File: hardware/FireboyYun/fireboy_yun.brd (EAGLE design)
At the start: 47.9 x 68.6 mm, 17 parts

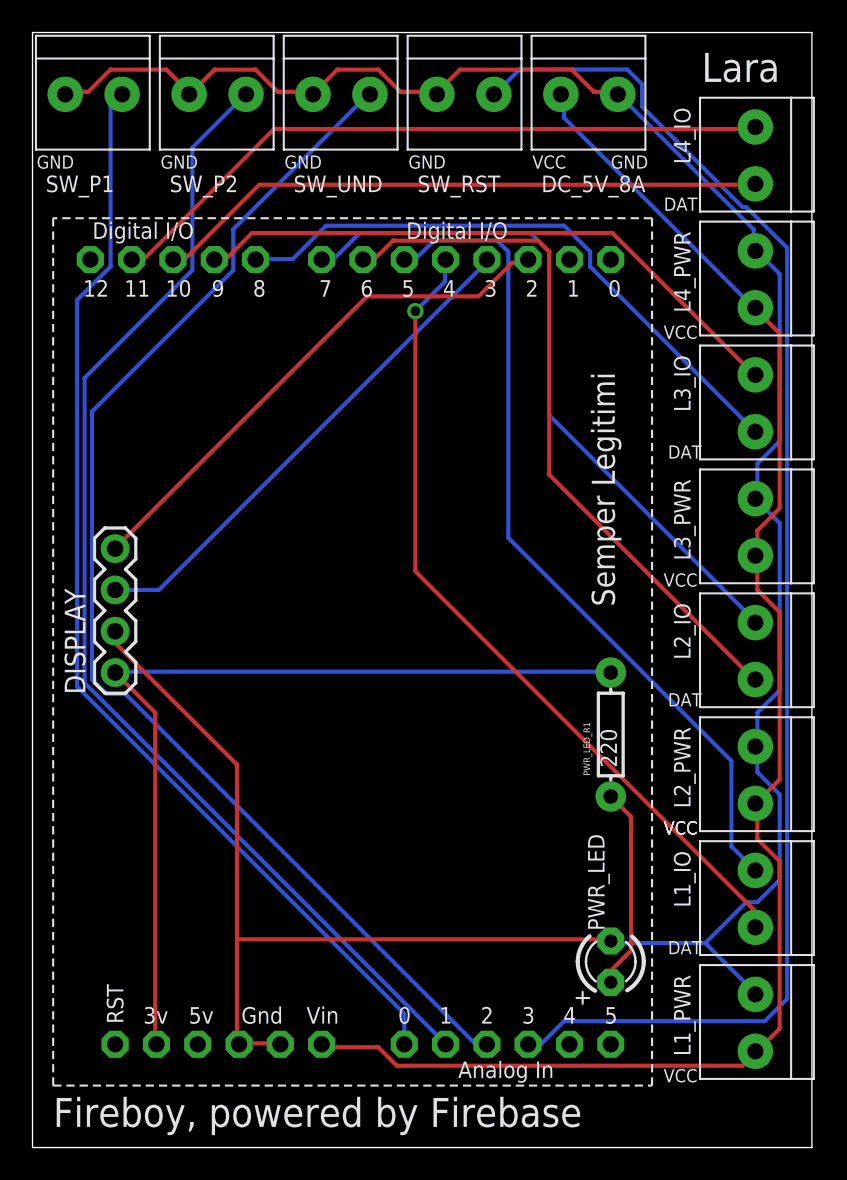
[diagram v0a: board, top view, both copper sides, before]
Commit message: hardware/FireboyYun: fix DRC error
- move upper terminal block right
- ripup; and autoroute
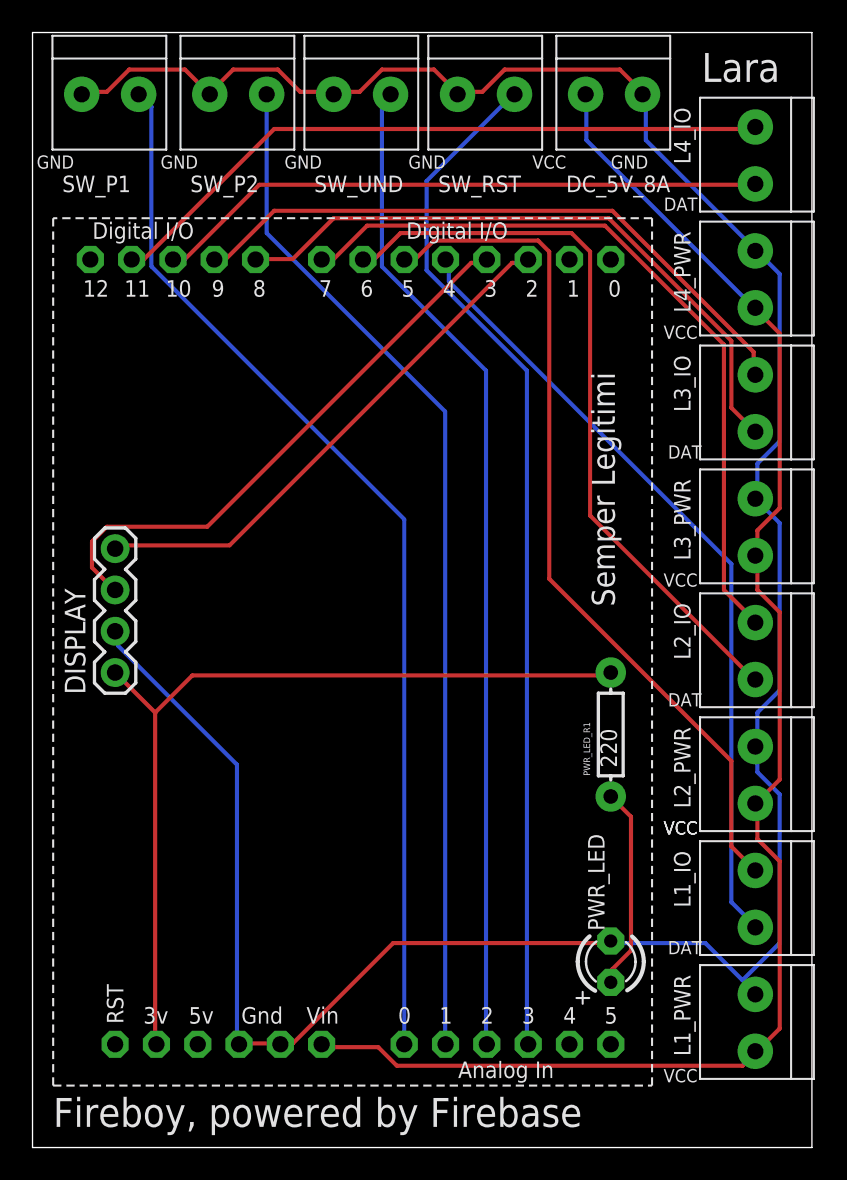
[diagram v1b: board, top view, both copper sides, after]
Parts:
- moved DC_5V_8A 1.52 mm to (35.8, 76.2)
- moved SW_P2 1.27 mm to (12.7, 76.2)
- moved SW_RST 1.27 mm to (27.9, 76.2)
- moved SW_UND 1.27 mm to (20.3, 76.2)
- moved SW_P1 1.02 mm to (4.83, 76.2)
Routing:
- net SW_RST: track 87.3 -> 63.3 mm
- net SW_UND: track 76.7 -> 61.3 mm
- net SW_P2: track 71.7 -> 63.0 mm
- net I2C_SCL: track 31.4 -> 35.1 mm
- net L2_CLK: track 43.2 -> 46.5 mm
- net SW_P1: track 67.9 -> 65.2 mm
- net L3_DAT: track 37.4 -> 39.6 mm
- net L3_CLK: track 37.5 -> 39.5 mm
- net L2_DAT: track 43.8 -> 45.7 mm
- net L1_DAT: track 50.5 -> 48.9 mm, vias 1 -> 0
- net L1_CLK: track 51.5 -> 53.0 mm
- net 3.3V: track 54.4 -> 53.0 mm
- net GND: track 164.9 -> 165.6 mm
- net VCC: track 95.4 -> 94.7 mm
